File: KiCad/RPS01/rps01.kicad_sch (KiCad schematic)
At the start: 10 parts, among them J1 XT90 IN BAT1, J2 XT90 IN BAT2, J3 XT90 ESC Output, J4 XT30PW Out Orin, J5 3x XT60 Template, J5 MCU_prog_header, J6 MCU_ICSP_header, J6 XT30PW Bat Out, J7 JST_PH_MCU_I2C, U9 L78M05CDT-TR 5V Reg

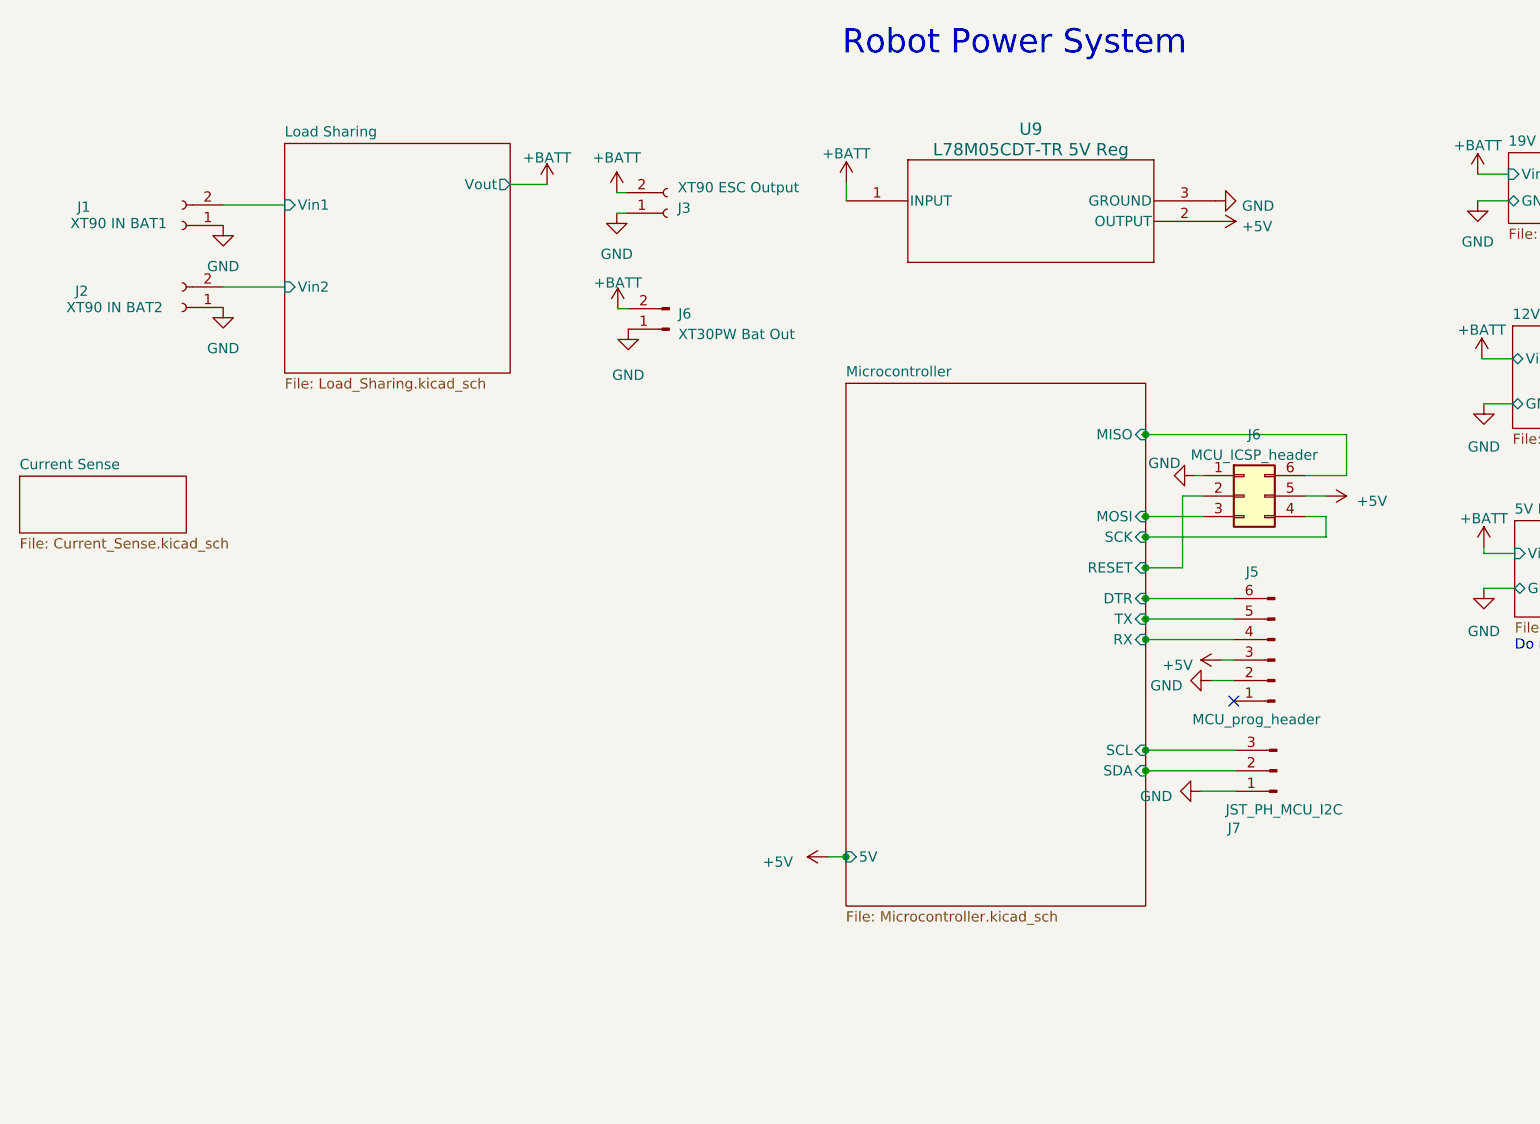
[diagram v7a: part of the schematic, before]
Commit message: Added Voltmeter
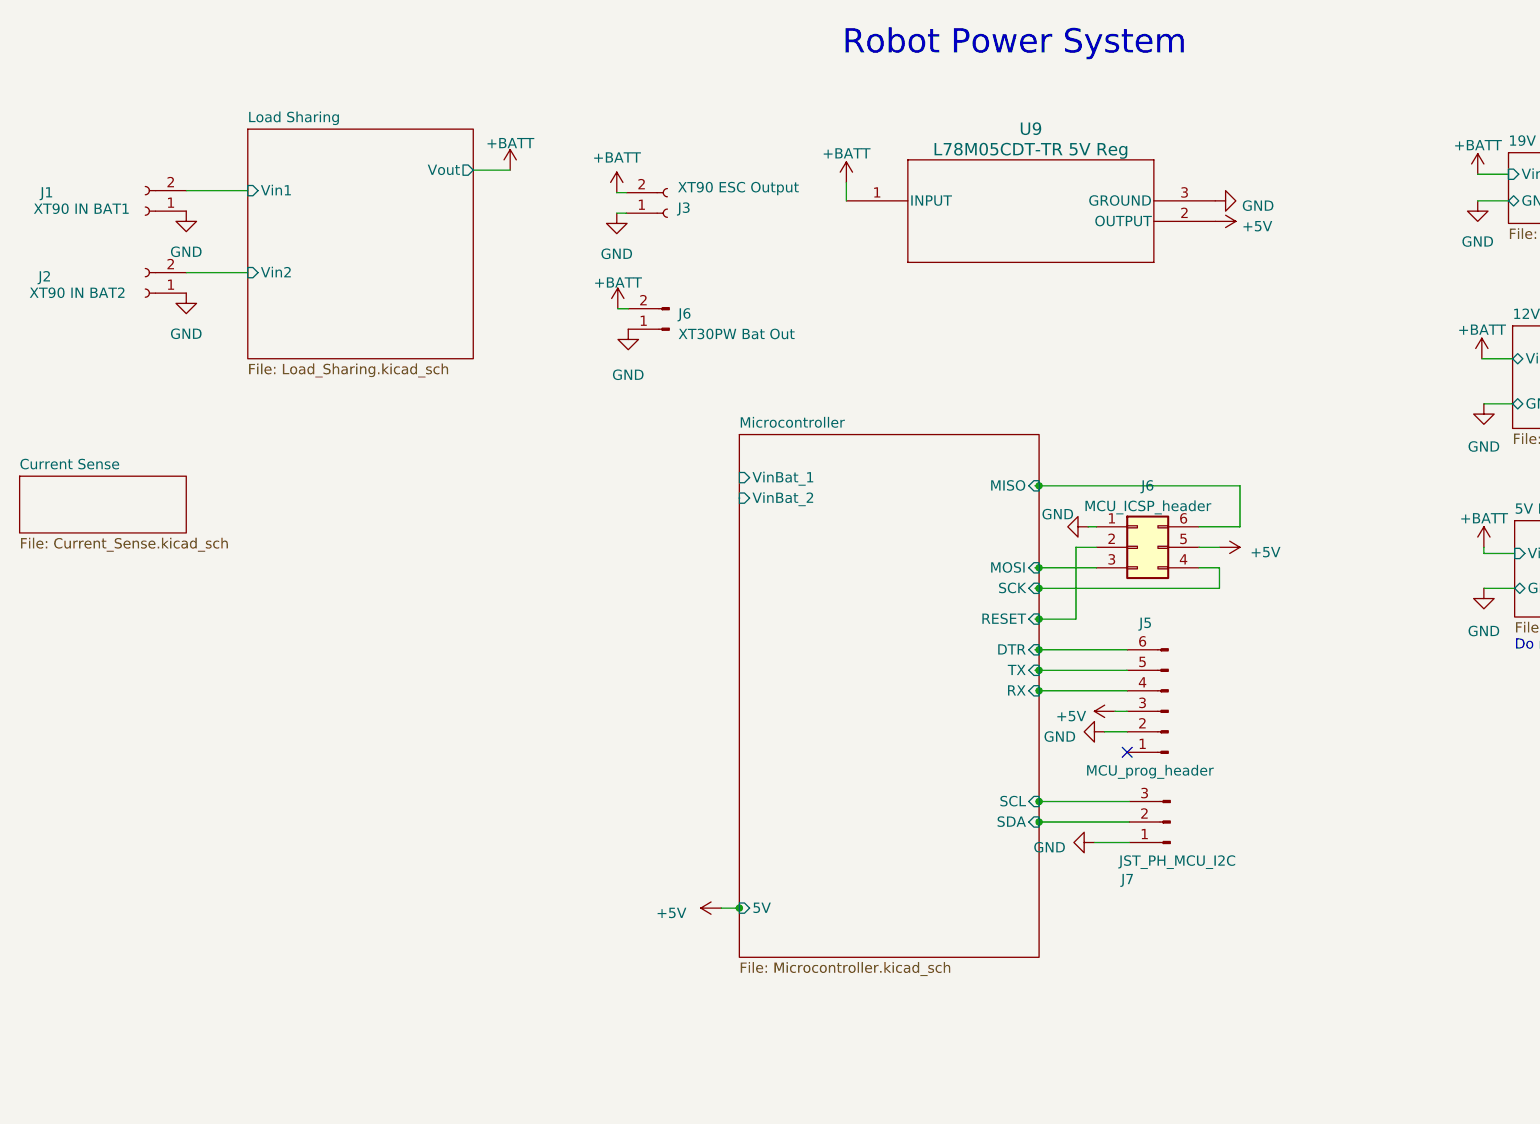
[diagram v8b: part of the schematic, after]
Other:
- sheet Microcontroller ports: added VinBat_1, VinBat_2; removed none
- moved on the sheet: J1, J2, J5, J6, J7
